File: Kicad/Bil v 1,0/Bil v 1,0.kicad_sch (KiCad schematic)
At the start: 2 parts, among them J1 Analog, J2 Digital

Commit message: Buggy car sch 1.0
Schematic for buggy car, probably correct
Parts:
- added BT1: Battery, symbol Device:Battery
- added J3, J4, J6: Lidar_sensor_adafruit_VL53L0X, symbol Auto_car_library:Lidar_sensor_adafruit_VL53L0X
- added M1: Motor_DC, symbol Motor:Motor_DC
- added M2: Motor_Servo, symbol Motor:Motor_Servo
- added R1, R2: 4,7 kΩ, Resistor_THT:R_Axial_DIN0207_L6.3mm_D2.5mm_P7.62mm_Horizontal, symbol Device:R
- added U1: ~, symbol Auto_car_library:Motron_i2c_3motor
- added U2: ~, symbol Auto_car_library:DC-DC
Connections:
- net *D9: now also M2.1 (PWM)
- net +3V3: now also J3.1 (Vin), J4.1 (Vin), J6.1 (Vin), U1.7 (Vdd)
- net +5V: now also M2.2 (+), R1.2, R2.2
- net A4/SDA: now also J3.4 (SDA), J4.4 (SDA), J6.4 (SDA), R2.1, U1.6 (SDA)
- net A5/SCL: now also J3.3 (SCL), J4.3 (SCL), J6.3 (SCL), R1.1, U1.5 (SCL)
- net GND: now also BT1.2 (-), J3.2 (GND), J4.2 (GND), J6.2 (GND), M2.3 (-), U1.11 (Gnd), U1.8 (Gnd), U2.2 (in_-), U2.4 (Out_-)
- net VCC: now also BT1.1 (+), U2.1 (in_+)
- new net DC-DC out: U1.10 (Vin), U2.3 (Out_+)
- new net M1 +: M1.1 (+), U1.12 (M1a)
- new net M1 -: M1.2 (-), U1.13 (M1b)
- no-connect marks 0 -> 35
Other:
- company: (none) -> Yrgo
- title: (none) -> Buggy v1.0

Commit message: updated resistor values
Updated values for I2C resistors so that it (probably) will work with 400 kHz speeds
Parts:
- R1, R2: value 4,7 kΩ -> 1,3 kΩ
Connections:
- net +3V3: now also R1.2, R2.2
- net +5V: no longer R1.2, R2.2
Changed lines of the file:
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@@
-	)
-	(symbol
-		(lib_id "power:+5V")
-		(at 142.24 81.28 0)
-		(unit 1)
-		(exclude_from_sim no)
-		(in_bom yes)
-		(on_board yes)
-		(dnp no)
-		(property "Reference" "#PWR016"
-			(at 142.24 85.09 0)
-			(effects
-				(font
-					(size 1.27 1.27)
-				)
-				(hide yes)
-			)
-		)
-		(property "Value" "+5V"
-			(at 142.24 77.724 90)
-			(effects
-				(font
-					(size 1.27 1.27)
-				)
-				(justify left)
-			)
-		)
-		(property "Footprint" ""
-			(at 142.24 81.28 0)
-			(effects
-				(font
-					(size 1.27 1.27)
-				)
-				(hide yes)
-			)
-		)
-		(property "Datasheet" ""
-			(at 142.24 81.28 0)
-			(effects
-				(font
-					(size 1.27 1.27)
-				)
-				(hide yes)
-			)
-		)
-		(property "Description" "Power symbol creates a global label with name \"+5V\""
-			(at 142.24 81.28 0)
-			(effects
-				(font
-					(size 1.27 1.27)
-				)
-				(hide yes)
-			)
-		)
-		(pin "1"
-		)
-		(instances
-			(project "Bil v 1,0"
-				(path "/0d35483a-0b12-46cc-b9f2-896fd6831779"
-					(reference "#PWR016")
-					(unit 1)
-				)
-			)
-		)
 	)
 	(symbol
@@
 			)
 		)
-		(property "Value" "4,7 kΩ"
+		(property "Value" "1,3 kΩ"
 			(at 130.81 77.47 90)
 			(effects
@@
 				(path "/0d35483a-0b12-46cc-b9f2-896fd6831779"
 					(reference "#PWR012")
+					(unit 1)
+				)
+			)
+		)
+	)
+	(symbol
+		(lib_id "power:+3.3V")
+		(at 142.24 81.28 0)
+		(unit 1)
+		(exclude_from_sim no)
+		(in_bom yes)
+		(on_board yes)
+		(dnp no)
+		(property "Reference" "#PWR016"
+			(at 142.24 85.09 0)
+			(effects
+				(font
+					(size 1.27 1.27)
+				)
+				(hide yes)
+			)
+		)
+		(property "Value" "+3V3"
+			(at 142.24 77.724 90)
+			(effects
+				(font
+					(size 1.27 1.27)
+				)
+				(justify left)
+			)
+		)
+		(property "Footprint" ""
+			(at 142.24 81.28 0)
+			(effects
+				(font
+					(size 1.27 1.27)
+				)
+				(hide yes)
+			)
+		)
+		(property "Datasheet" ""
+			(at 142.24 81.28 0)
+			(effects
+				(font
+					(size 1.27 1.27)
+				)
+				(hide yes)
+			)
+		)
+		(property "Description" "Power symbol creates a global label with name \"+3.3V\""
+			(at 142.24 81.28 0)
+			(effects
+				(font
+					(size 1.27 1.27)
+				)
+				(hide yes)
+			)
+		)
+		(pin "1"
+		)
+		(instances
+			(project "Bil v 1,0"
+				(path "/0d35483a-0b12-46cc-b9f2-896fd6831779"
+					(reference "#PWR016")
 					(unit 1)
 				)
@@
 			)
 		)
-		(property "Value" "4,7 kΩ"
+		(property "Value" "1,3 kΩ"
 			(at 130.81 87.63 90)
 			(effects

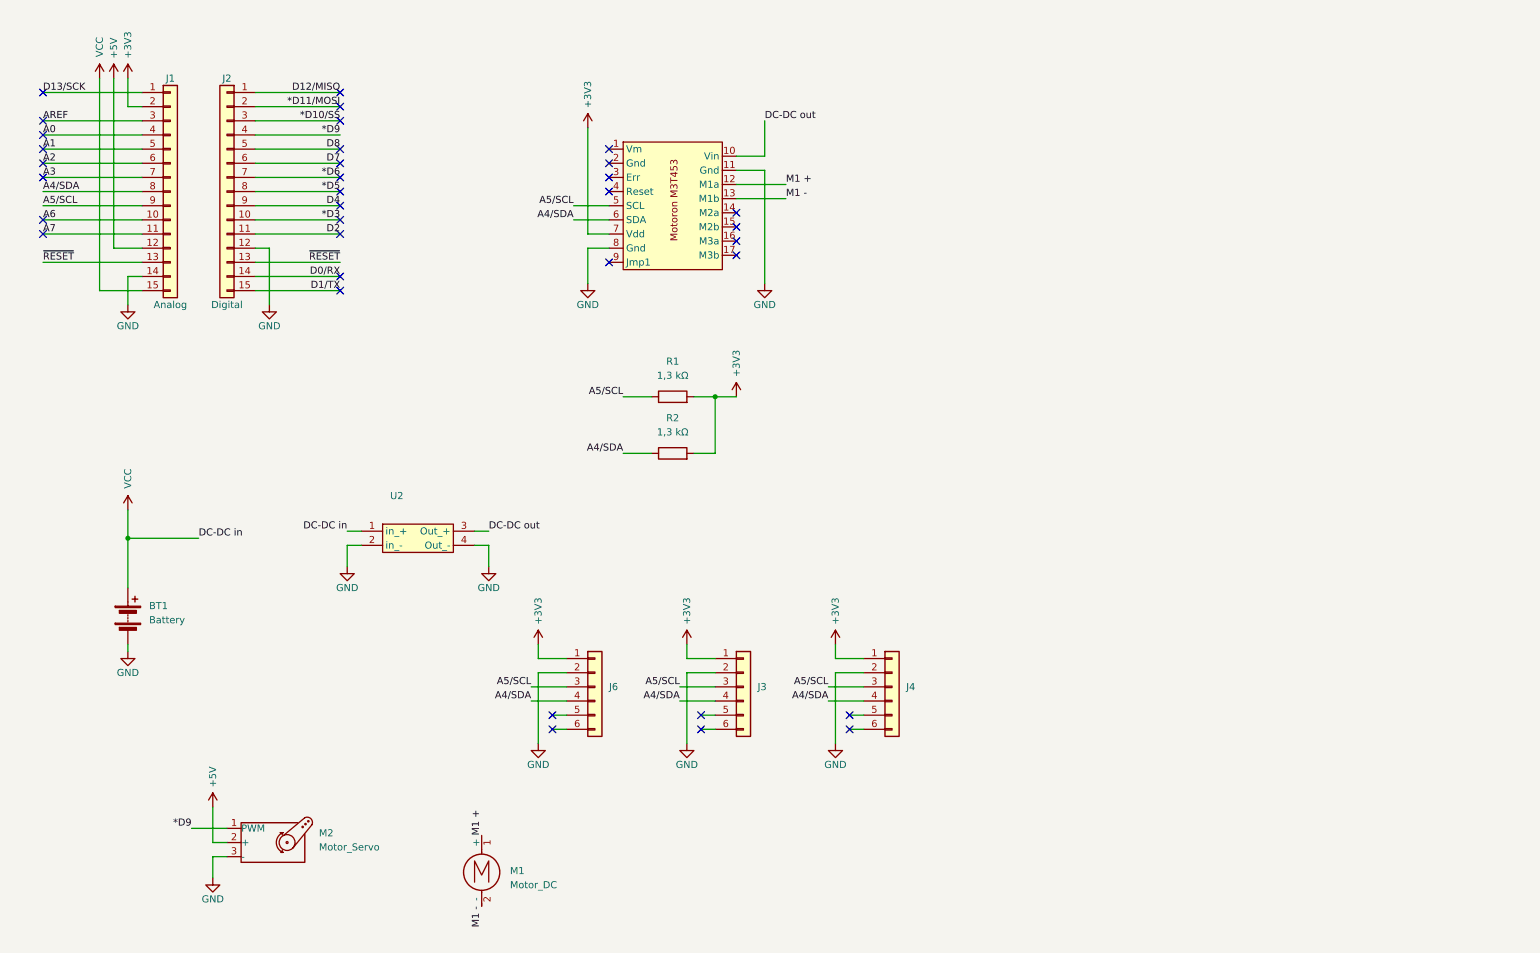
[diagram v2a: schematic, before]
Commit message: motor layous for the other cars
added schematics for how motors on the digger and g-wagon should be connected
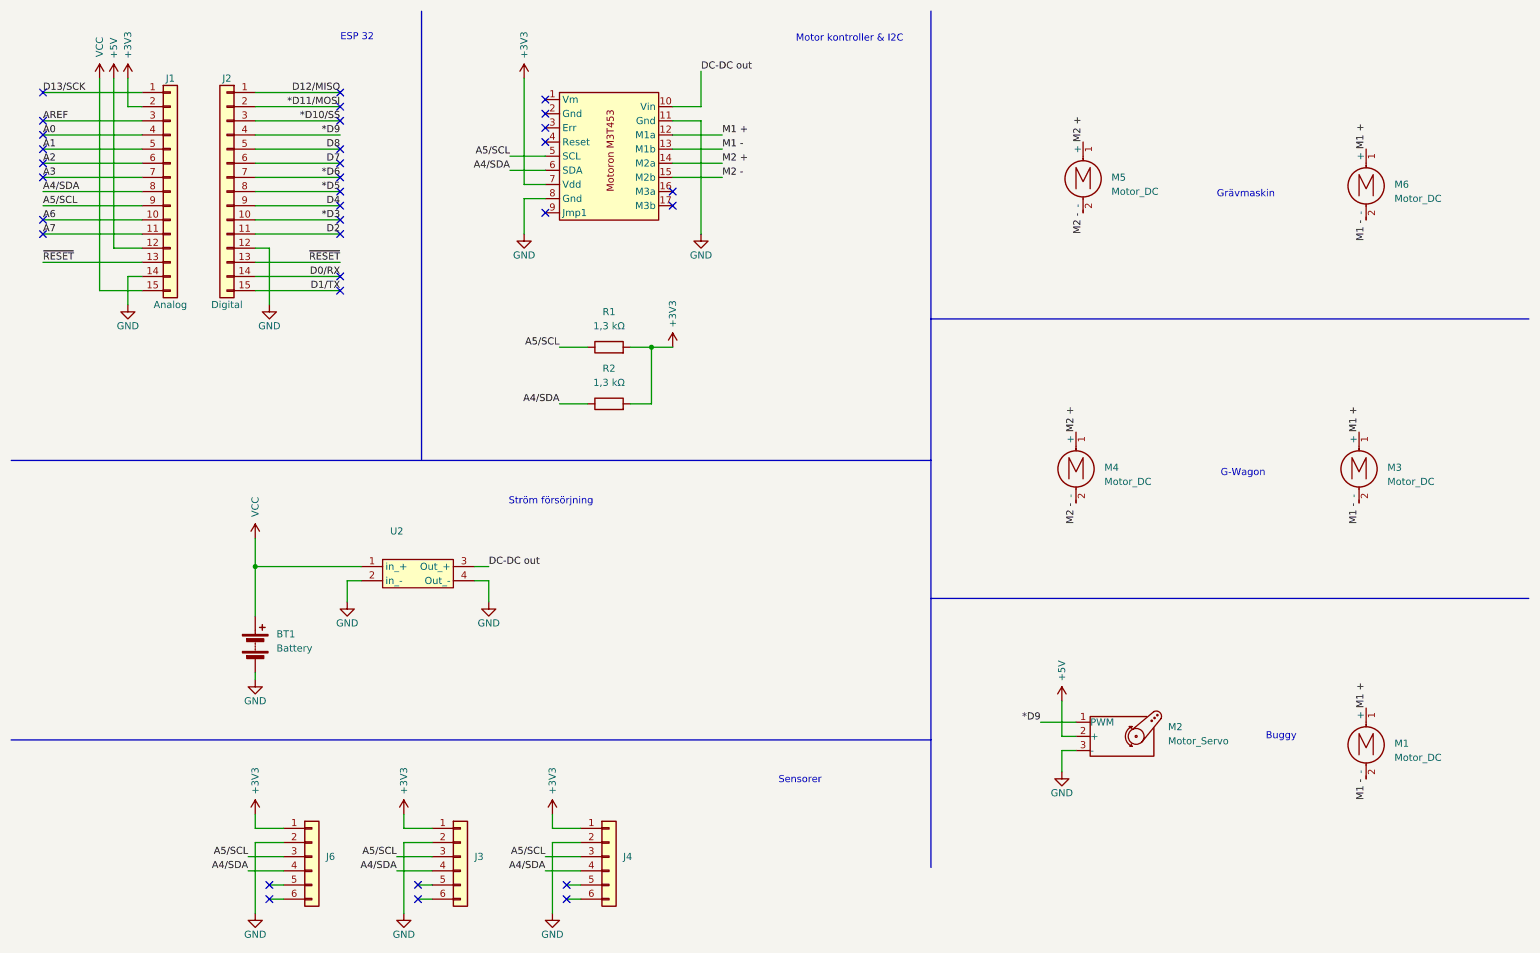
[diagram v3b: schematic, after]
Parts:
- added M3, M4, M5, M6: Motor_DC, symbol Motor:Motor_DC
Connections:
- net M1 +: now also M3.1 (+), M6.1 (+)
- net M1 -: now also M3.2 (-), M6.2 (-)
- net M2 +: now reaches U1.14 (M2a)
- net M2 +: now also M4.1 (+), M5.1 (+)
- net M2 -: now reaches U1.15 (M2b)
- net M2 -: now also M4.2 (-), M5.2 (-)
- no-connect marks 35 -> 33
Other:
- note added: "Buggy"
- note added: "ESP 32"
- note added: "G-Wagon"
- note added: "Grävmaskin"
- note added: "Motor kontroller & I2C"
- note added: "Sensorer"
- note added: "Ström försörjning"
- title: Buggy v1.0 -> C++? I hardly know her
- moved on the sheet: BT1, J3, J4, J6, M1, M2, R1, R2, U2

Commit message: pcb layouyt1.0
first draft of pcb layout
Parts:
- removed M5, M6: Motor_DC, symbol Motor:Motor_DC
- added J5: Conn_01x04, Connector_PinSocket_2.54mm:PinSocket_1x04_P2.54mm_Vertical, symbol Connector_Generic:Conn_01x04
- BT1: footprint (none) -> Connector_JST:JST_EH_B2B-EH-A_1x02_P2.50mm_Vertical
- J3, J4, J6: footprint (none) -> Connector_PinHeader_2.54mm:PinHeader_1x06_P2.54mm_Vertical
- M1, M4: footprint (none) -> Connector_JST:JST_PH_B2B-PH-K_1x02_P2.00mm_Vertical
- M2: footprint (none) -> Connector_JST:JST_PH_B3B-PH-K_1x03_P2.00mm_Vertical
- U1: value ~ -> (none); footprint (none) -> Auto_car:Motron motorcontroller 2 motor
- U2: value ~ -> (none); footprint (none) -> Auto_car:DC_DC
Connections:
- net *D3: now also J4.6 (Xshut)
- net *D5: now also J6.6 (Xshut)
- net +3V3: now also J5.1 (Pin_1)
- net +5V: no longer M2.2 (+)
- net D4: now also J3.6 (Xshut)
- net D8: now also J5.3 (Pin_3)
- net DC-DC out: now also M2.2 (+), U1.12 (Vin); no longer U1.10 (Vin)
- net GND: now also U1.13 (Gnd), J5.2 (Pin_2); no longer U1.11 (Gnd)
- net M1 +: now also U1.10 (M1b); no longer U1.12 (M1a)
- net M1 -: now also U1.11 (M1a); no longer U1.13 (M1b)
- no-connect marks 33 -> 25
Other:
- note added: "G-Wagon / Grävmaskin"
- note added: "Start modul"
- note removed: "G-Wagon"
- note removed: "Grävmaskin"
- moved on the sheet: BT1, U2

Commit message: 1.3 updated layout
the probably final board layout, now with power switch
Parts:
- added SW2: power switch, Button_Switch_THT:SW_Slide-03_Wuerth-WS-SLTV_10x2.5x6.4_P2.54mm, symbol Switch:SW_Nidec_CAS-120A1
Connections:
- net VCC: now also SW2.1 (C); no longer BT1.1 (+)
- new net: BT1.1 (+), SW2.2 (B)
- no-connect marks 25 -> 26
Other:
- moved on the sheet: BT1, U2

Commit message: 1.4.1 updated silkscreens
updated silkscreens with names of modules
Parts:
- renumbered M4 to M2, M2 to Servo
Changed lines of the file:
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@@
 		(dnp no)
 		(fields_autoplaced yes)
-		(property "Reference" "M2"
+		(property "Reference" "Servo"
 			(at 219.71 140.5368 0)
 			(show_name no)
@@
 			(project "Bil v 1,0"
 				(path "/0d35483a-0b12-46cc-b9f2-896fd6831779"
-					(reference "M2")
+					(reference "Servo")
 					(unit 1)
 				)
@@
 		(dnp no)
 		(fields_autoplaced yes)
-		(property "Reference" "M4"
+		(property "Reference" "M2"
 			(at 208.28 93.9799 0)
 			(show_name no)
@@
 			(project "Bil v 1,0"
 				(path "/0d35483a-0b12-46cc-b9f2-896fd6831779"
-					(reference "M4")
-					(unit 1)
-				)
+					(reference "M2")
+					(unit 1)
+				)
